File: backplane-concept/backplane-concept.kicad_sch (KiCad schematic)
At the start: 2 parts

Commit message: Rev
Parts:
- removed J2: ~, !footprints:9-1734774-5, symbol 9-1734774-5:PCIE
- added J2: CONN_MINI, CONN_10018784-10201TLF, symbol 10018784-10201TLF:10018784-10201TLF
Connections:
- net RX3 is gone; now on net GND: J1.B23
- net TX2 is gone; now on net GND: J1.B20
- net TX3 is gone; now on net I2C0_ECVT: J1.B22
- net DIR1: no longer J1.A14
- net DIR2: no longer J1.A13
- net ENGHALL2: no longer J1.A20
- net FRBPRESS: no longer J1.B43
- net GND: now also J1.A16, J1.A18, J1.A32; no longer J1.A17, J1.A21, J1.A38, J1.A45, J1.B28, J1.B42
- net PENC_A: no longer J1.A30
- net PENC_B: no longer J1.A32
- net PLDCLK: no longer J1.A24
- net PLDDAT: no longer J1.A25
- net PLOADC1: no longer J1.A22
- net PLOADC2: no longer J1.A23
- net PWM1: no longer J1.A16
- net PWM2: no longer J1.A15
- net RPOT1: no longer J1.B45
- net RPOT2: no longer J1.B46
- net RRBPRESS: no longer J1.B44
- net RRHALL: now also J1.A13; no longer J1.A19
- net SENC_A: no longer J1.A34
- net SENC_B: no longer J1.A36
- net SLDCLK: no longer J1.A28
- net SLDDAT: no longer J1.A29
- net SLOADC1: no longer J1.A26
- net SLOADC2: no longer J1.A27
- net SPARK: no longer J1.A18
- net TEMP1: no longer J1.A49
- net TEMP2: no longer J1.A48
- net TEMP3: no longer J1.A47
- net TEMP4: no longer J1.A46
- net VOLT1: now also J1.A29; no longer J1.B47
- net VOLT2: now also J1.A30; no longer J1.B48
- net VOLT3: now also J1.A31; no longer J1.B49
- net ~PENC_A: no longer J1.A31
- net ~PENC_B: no longer J1.A33
- net ~SENC_A: no longer J1.A35
- net ~SENC_B: no longer J1.A37
- net 3.3V renamed +3V3
- net 5V renamed +5V
- net 8.4V renamed +8V
- net CIPO: no longer names the net of J1.B29
- net COPI: no longer names the net of J1.B30
- net CS1: no longer names the net of J1.B32
- removed net CS2: J1.B33
- removed net CS3: J1.B34
- removed net CS4: J1.B35
- removed net CS5: J1.B36
- removed net CS6: J1.B37
- removed net DIG_OUT: J1.A39
- net I2C_CLK renamed I2C0_DAQ_SCL
- net I2C_DATA renamed I2C0_DAQ_SDA
- removed net IR_AMP: J1.A42
- removed net IR_TEENSY: J1.A41
- removed net N_A: J1.A40
- net RX1 renamed I2C1_DAQ_SCL
- net RX2 renamed I2C0_ECVT
- net RX4: no longer names the net of J1.B25
- net RX5: no longer names the net of J1.B27
- net SCLK: no longer names the net of J1.B31
- net TX1 renamed I2C1_DAQ_SDA
- net TX4: no longer names the net of J1.B24
- net TX5: no longer names the net of J1.B26
- new net ARGB_DAQ: J1.A20
- new net ARGB_ECVT: J1.A19
- new net ARGB_ESP: J1.A21
- new net DAQ_RX0_ECVT_TX0: J1.A15
- new net DAQ_TX0_ECVT_RX0: J1.A14
- new net DAQ_TX1_DATA: J1.A17

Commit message: Backplane Ideas
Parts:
- removed J1: ~, !footprints:9-1734774-5, symbol 9-1734774-5:PCIE
- removed J2: CONN_MINI, CONN_10018784-10201TLF, symbol 10018784-10201TLF:10018784-10201TLF
- added J1: 6473427-1, 64734271, symbol 6473427-1:6473427-1
- added J2, J3, J4: PCIE_8x_Labeled, !footprints:9-1734774-5, symbol !CUSTOM:PCIE_8x_Labeled
- added J5, J6, J7, J8: CONN_MINI, !footprints:10018784-10200TLF, symbol !CUSTOM:PCIE_2x_Labeled
- added U4: ATA6561-GBQW-N, VDFN8_3X3_MCH, symbol ATA6561:ATA6561-GBQW-N
- added U5: ESP32-PICO-D4, Package_DFN_QFN:QFN-48-1EP_7x7mm_P0.5mm_EP5.3x5.3mm, symbol RF_Module:ESP32-PICO-D4
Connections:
- net +3V3: now also J1.B10, J1.B25, J1.B26, J2.A4 (+3V3), J2.A5 (+3V3), J2.A6 (+3V3), J2.B4 (+3V3), J2.B5 (+3V3), J2.B6 (+3V3), J3.A4 (+3V3), J3.A5 (+3V3), J3.A6 (+3V3), J3.B4 (+3V3), J3.B5 (+3V3), J3.B6 (+3V3), J4.A4 (+3V3), J4.A5 (+3V3), J4.A6 (+3V3), J4.B4 (+3V3), J4.B5 (+3V3), J4.B6 (+3V3), J5.A4 (+3V3), J5.A5 (+3V3), J5.A6 (+3V3), J5.B4 (+3V3), J5.B5 (+3V3), J5.B6 (+3V3), J6.A4 (+3V3), J6.A5 (+3V3), J6.A6 (+3V3), J6.B4 (+3V3), J6.B5 (+3V3), J6.B6 (+3V3), J7.A4 (+3V3), J7.A5 (+3V3), J7.A6 (+3V3), J7.B4 (+3V3), J7.B5 (+3V3), J7.B6 (+3V3), J8.A4 (+3V3), J8.A5 (+3V3), J8.A6 (+3V3), J8.B4 (+3V3), J8.B5 (+3V3), J8.B6 (+3V3)
- net +5V: now also J1.A1, J1.A10, J1.A18, J1.A26, J2.A1 (+5V), J2.A2 (+5V), J2.A3 (+5V), J2.B1 (+5V), J2.B2 (+5V), J2.B3 (+5V), J3.A1 (+5V), J3.A2 (+5V), J3.A3 (+5V), J3.B1 (+5V), J3.B2 (+5V), J3.B3 (+5V), J4.A1 (+5V), J4.A2 (+5V), J4.A3 (+5V), J4.B1 (+5V), J4.B2 (+5V), J4.B3 (+5V), J5.A1 (+5V), J5.A2 (+5V), J5.A3 (+5V), J5.B1 (+5V), J5.B2 (+5V), J5.B3 (+5V), J6.A1 (+5V), J6.A2 (+5V), J6.A3 (+5V), J6.B1 (+5V), J6.B2 (+5V), J6.B3 (+5V), J7.A1 (+5V), J7.A2 (+5V), J7.A3 (+5V), J7.B1 (+5V), J7.B2 (+5V), J7.B3 (+5V), J8.A1 (+5V), J8.A2 (+5V), J8.A3 (+5V), J8.B1 (+5V), J8.B2 (+5V), J8.B3 (+5V)
- net +8V: now also J1.B5, J1.B6, J2.A7 (VBATT), J2.A8 (VBATT), J2.B7 (VBATT), J2.B8 (VBATT), J3.A7 (VBATT), J3.A8 (VBATT), J3.B7 (VBATT), J3.B8 (VBATT), J4.A7 (VBATT), J4.A8 (VBATT), J4.B7 (VBATT), J4.B8 (VBATT), J5.A7 (VBATT), J5.A8 (VBATT), J5.B7 (VBATT), J5.B8 (VBATT), J6.A7 (VBATT), J6.A8 (VBATT), J6.B7 (VBATT), J6.B8 (VBATT), J7.A7 (VBATT), J7.A8 (VBATT), J7.B7 (VBATT), J7.B8 (VBATT), J8.A7 (VBATT), J8.A8 (VBATT), J8.B7 (VBATT), J8.B8 (VBATT)
- net CAN_H: now also J2.B12 (CAN_H), J3.B12 (CAN_H), J4.B12 (CAN_H), J5.B12 (CAN_H), J6.B12 (CAN_H), J7.B12 (CAN_H), J8.B12 (CAN_H)
- net CAN_L: now also J2.B13 (CAN_L), J3.B13 (CAN_L), J4.B13 (CAN_L), J5.B13 (CAN_L), J6.B13 (CAN_L), J7.B13 (CAN_L), J8.B13 (CAN_L)
- net DAQ_RX0_ECVT_TX0: now also J2.A13 (DAQ_RX0_ECVT_TX0), J3.A13 (DAQ_RX0_ECVT_TX0), J4.A13 (DAQ_RX0_ECVT_TX0), J5.A13 (DAQ_RX0_ECVT_TX0), J6.A13 (DAQ_RX0_ECVT_TX0), J7.A13 (DAQ_RX0_ECVT_TX0), J8.A13 (DAQ_RX0_ECVT_TX0)
- net DAQ_TX0_ECVT_RX0: now also J2.A12 (DAQ_TX0_ECVT_RX0), J3.A12 (DAQ_TX0_ECVT_RX0), J4.A12 (DAQ_TX0_ECVT_RX0), J5.A12 (DAQ_TX0_ECVT_RX0), J6.A12 (DAQ_TX0_ECVT_RX0), J7.A12 (DAQ_TX0_ECVT_RX0), J8.A12 (DAQ_TX0_ECVT_RX0)
- net DAQ_TX1_DATA: now also J2.A14 (DAQ_TX1_DATA), J3.A14 (DAQ_TX1_DATA), J4.A14 (DAQ_TX1_DATA), J5.A14 (DAQ_TX1_DATA), J6.A14 (DAQ_TX1_DATA), J7.A14 (DAQ_TX1_DATA), J8.A14 (DAQ_TX1_DATA)
- net GND: now also J1.A17, J1.A25, J1.A30, J1.A5, J1.B1, J1.B11, J1.B12, J1.B15, J1.B19, J1.B2, J1.B23, J1.B24, J1.B7, J2.A10 (GND), J2.A11 (GND), J2.A15 (GND), J2.A18 (GND), J2.A28 (GND), J2.A35 (GND), J2.A43 (GND), J2.A9 (GND), J2.B10 (GND), J2.B11 (GND), J2.B18 (GND), J2.B32 (GND), J2.B42 (GND), J2.B43 (GND), J2.B9 (GND), J3.A10 (GND), J3.A11 (GND), J3.A15 (GND), J3.A18 (GND), J3.A28 (GND), J3.A35 (GND), J3.A43 (GND), J3.A9 (GND), J3.B10 (GND), J3.B11 (GND), J3.B18 (GND), J3.B32 (GND), J3.B42 (GND), J3.B43 (GND), J3.B9 (GND), J4.A10 (GND), J4.A11 (GND), J4.A15 (GND), J4.A18 (GND), J4.A28 (GND), J4.A35 (GND), J4.A43 (GND), J4.A9 (GND), J4.B10 (GND), J4.B11 (GND), J4.B18 (GND), J4.B32 (GND), J4.B42 (GND), J4.B43 (GND), J4.B9 (GND), J5.A10 (GND), J5.A11 (GND), J5.A15 (GND), J5.A18 (GND), J5.A9 (GND), J5.B10 (GND), J5.B11 (GND), J5.B18 (GND), J5.B9 (GND), J6.A10 (GND), J6.A11 (GND), J6.A15 (GND), J6.A18 (GND), J6.A9 (GND), J6.B10 (GND), J6.B11 (GND), J6.B18 (GND), J6.B9 (GND), J7.A10 (GND), J7.A11 (GND), J7.A15 (GND), J7.A18 (GND), J7.A9 (GND), J7.B10 (GND), J7.B11 (GND), J7.B18 (GND), J7.B9 (GND), J8.A10 (GND), J8.A11 (GND), J8.A15 (GND), J8.A18 (GND), J8.A9 (GND), J8.B10 (GND), J8.B11 (GND), J8.B18 (GND), J8.B9 (GND)
- net I2C0_DAQ_SCL: now also J2.B15 (I2C0_DAQ_SCL), J3.B15 (I2C0_DAQ_SCL), J4.B15 (I2C0_DAQ_SCL), J5.B15 (I2C0_DAQ_SCL), J6.B15 (I2C0_DAQ_SCL), J7.B15 (I2C0_DAQ_SCL), J8.B15 (I2C0_DAQ_SCL)
- net I2C0_DAQ_SDA: now also J2.B14 (I2C0_DAQ_SDA), J3.B14 (I2C0_DAQ_SDA), J4.B14 (I2C0_DAQ_SDA), J5.B14 (I2C0_DAQ_SDA), J6.B14 (I2C0_DAQ_SDA), J7.B14 (I2C0_DAQ_SDA), J8.B14 (I2C0_DAQ_SDA)
- net I2C1_DAQ_SCL: now also J2.A17 (I2C1_DAQ_SCL), J3.A17 (I2C1_DAQ_SCL), J4.A17 (I2C1_DAQ_SCL), J5.A17 (I2C1_DAQ_SCL), J6.A17 (I2C1_DAQ_SCL), J7.A17 (I2C1_DAQ_SCL), J8.A17 (I2C1_DAQ_SCL)
- net I2C1_DAQ_SDA: now also J2.A16 (I2C1_DAQ_SDA), J3.A16 (I2C1_DAQ_SDA), J4.A16 (I2C1_DAQ_SDA), J5.A16 (I2C1_DAQ_SDA), J6.A16 (I2C1_DAQ_SDA), J7.A16 (I2C1_DAQ_SDA), J8.A16 (I2C1_DAQ_SDA)
- net RPOT1: now also J2.B46 (RPOT1), J3.B46 (RPOT1), J4.B46 (RPOT1)
- net RPOT2: now also J2.B47 (RPOT2), J3.B47 (RPOT2), J4.B47 (RPOT2)
- net SPARK: now also J2.A42 (SPARK), J3.A42 (SPARK), J4.A42 (SPARK)
- new net: U5.1 (VDDA), U5.43 (VDDA), U5.46 (VDDA)
- new net: U5.3 (VDDA3P3), U5.4 (VDDA3P3)
- new net: J2.A19, J3.A19, J4.A19
- new net: J2.A20, J3.A20, J4.A20
- new net: J2.A21, J3.A21, J4.A21
- new net: J2.A22, J3.A22, J4.A22
- new net: J2.A23, J3.A23, J4.A23
- new net: J2.A24, J3.A24, J4.A24
- new net: J2.A25, J3.A25, J4.A25
- new net: J2.A26, J3.A26, J4.A26
- new net: J2.A27, J3.A27, J4.A27
- new net: J2.B19, J3.B19, J4.B19
- new net: J2.B20, J3.B20, J4.B20
- new net: J2.B21, J3.B21, J4.B21
- new net: J2.B22, J3.B22, J4.B22
- new net: J2.B23, J3.B23, J4.B23
- new net: J2.B24, J3.B24, J4.B24
- new net: J2.B25, J3.B25, J4.B25
- new net: J2.B26, J3.B26, J4.B26
- new net: J2.B27, J3.B27, J4.B27
- new net: J2.B48, J3.B48, J4.B48
- new net: J2.B49, J3.B49, J4.B49
- new net AVDD_P: J1.B18
- new net AVDD_S: J1.B22
- new net BP_FRONT: J2.B44 (BP_FRONT), J3.B44 (BP_FRONT), J4.B44 (BP_FRONT)
- new net BP_REAR: J2.B45 (BP_REAR), J3.B45 (BP_REAR), J4.B45 (BP_REAR)
- new net DIR_P: J2.B36 (DIR_P), J3.B36 (DIR_P), J4.B36 (DIR_P)
- new net DIR_S: J2.B38 (DIR_S), J3.B38 (DIR_S), J4.B38 (DIR_S)
- new net ENCA_P: J1.A11, J2.A29 (ENCA_P), J3.A29 (ENCA_P), J4.A29 (ENCA_P)
- new net ENCA_S: J1.A19, J2.A36 (ENCA_S), J3.A36 (ENCA_S), J4.A36 (ENCA_S)
- new net ENCB_P: J1.A13, J2.A31 (ENCB_P), J3.A31 (ENCB_P), J4.A31 (ENCB_P)
- new net ENCB_S: J1.A21, J2.A38 (ENCB_S), J3.A38 (ENCB_S), J4.A38 (ENCB_S)
- new net ENCI_P: J1.A15, J2.A33 (ENCI_P), J3.A33 (ENCI_P), J4.A33 (ENCI_P)
- new net ENCI_S: J1.A23, J2.A40 (ENCI_S), J3.A40 (ENCI_S), J4.A40 (ENCI_S)
- new net HALL1_P: J1.A2
- new net HALL1_S: J1.A27
- new net HALL2_P: J1.A3
- new net HALL2_S: J1.A28
- new net HALL3_P: J1.A4
- new net HALL3_S: J1.A29
- new net HALL_ENG1: J1.B3, J2.B33 (HALL_ENG1), J3.B33 (HALL_ENG1), J4.B33 (HALL_ENG1)
- new net HALL_ENG2: J1.B4, J2.B41 (HALL_ENG2), J3.B41 (HALL_ENG2), J4.B41 (HALL_ENG2)
- new net HALL_RW: J2.B34 (HALL_RW), J3.B34 (HALL_RW), J4.B34 (HALL_RW)
- new net I2C0_ECVT_SCL: J2.B17 (I2C0_ECVT_SCL), J3.B17 (I2C0_ECVT_SCL), J4.B17 (I2C0_ECVT_SCL), J5.B17 (I2C0_ECVT_SCL), J6.B17 (I2C0_ECVT_SCL), J7.B17 (I2C0_ECVT_SCL), J8.B17 (I2C0_ECVT_SCL)
- new net I2C0_ECVT_SDA: J2.B16 (I2C0_ECVT_SDA), J3.B16 (I2C0_ECVT_SDA), J4.B16 (I2C0_ECVT_SDA), J5.B16 (I2C0_ECVT_SDA), J6.B16 (I2C0_ECVT_SDA), J7.B16 (I2C0_ECVT_SDA), J8.B16 (I2C0_ECVT_SDA)
- new net I2C1_ECVT_EXT_SCL: J1.B9, J2.B40 (I2C1_ECVT_EXT_SCL), J3.B40 (I2C1_ECVT_EXT_SCL), J4.B40 (I2C1_ECVT_EXT_SCL)
- new net I2C1_ECVT_EXT_SDA: J1.B8, J2.B39 (I2C1_ECVT_EXT_SDA), J3.B39 (I2C1_ECVT_EXT_SDA), J4.B39 (I2C1_ECVT_EXT_SDA)
- new net IN+_P: J1.B16
- new net IN+_S: J1.B20
- new net IN-_P: J1.B17
- new net IN-_S: J1.B21
- new net LOADC_CLK_P: J2.B28 (LOADC_CLK_P), J2.B30 (LOADC_CLK_S), J3.B28 (LOADC_CLK_P), J3.B30 (LOADC_CLK_S), J4.B28 (LOADC_CLK_P), J4.B30 (LOADC_CLK_S)
- new net LOADC_DAT_P: J2.B29 (LOADC_DAT_P), J3.B29 (LOADC_DAT_P), J4.B29 (LOADC_DAT_P)
- new net LOADC_DAT_S: J2.B31 (LOADC_DAT_S), J3.B31 (LOADC_DAT_S), J4.B31 (LOADC_DAT_S)
- new net MOT1_P: J1.A7
- new net MOT1_S: J1.A32
- new net MOT2_P: J1.A8
- new net MOT2_S: J1.A33
- new net MOT3_P: J1.A9
- new net MOT3_S: J1.A34
- new net PWM_P: J2.B35 (PWM_P), J3.B35 (PWM_P), J4.B35 (PWM_P)
- new net PWM_S: J2.B37 (PWM_S), J3.B37 (PWM_S), J4.B37 (PWM_S)
- new net THERM_A1_CASE: J1.B13, J2.A46 (THERM_A1_CASE), J3.A46 (THERM_A1_CASE), J4.A46 (THERM_A1_CASE)
- new net THERM_A2_CASE: J1.B14, J2.A47 (THERM_A2_CASE), J3.A47 (THERM_A2_CASE), J4.A47 (THERM_A2_CASE)
- new net THERM_A3: J2.A48 (THERM_A3), J3.A48 (THERM_A3), J4.A48 (THERM_A3)
- new net THERM_A4: J2.A49 (THERM_A4), J3.A49 (THERM_A4), J4.A49 (THERM_A4)
- new net THERM_P: J1.A6, J2.A44 (THERM_P), J3.A44 (THERM_P), J4.A44 (THERM_P)
- new net THERM_S: J1.A31, J2.A45 (THERM_S), J3.A45 (THERM_S), J4.A45 (THERM_S)
- new net ~ENCA_P: J1.A12, J2.A30 (~ENCA_P), J3.A30 (~ENCA_P), J4.A30 (~ENCA_P)
- new net ~ENCA_S: J1.A20, J2.A37 (~ENCA_S), J3.A37 (~ENCA_S), J4.A37 (~ENCA_S)
- new net ~ENCB_P: J1.A14, J2.A32 (~ENCB_P), J3.A32 (~ENCB_P), J4.A32 (~ENCB_P)
- new net ~ENCB_S: J1.A22, J2.A39 (~ENCB_S), J3.A39 (~ENCB_S), J4.A39 (~ENCB_S)
- new net ~ENCI_P: J1.A16, J2.A34 (~ENCI_P), J3.A34 (~ENCI_P), J4.A34 (~ENCI_P)
- new net ~ENCI_S: J1.A24, J2.A41 (~ENCI_S), J3.A41 (~ENCI_S), J4.A41 (~ENCI_S)
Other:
- added sheet Analog Frontend (analog_frontend.kicad_sch)

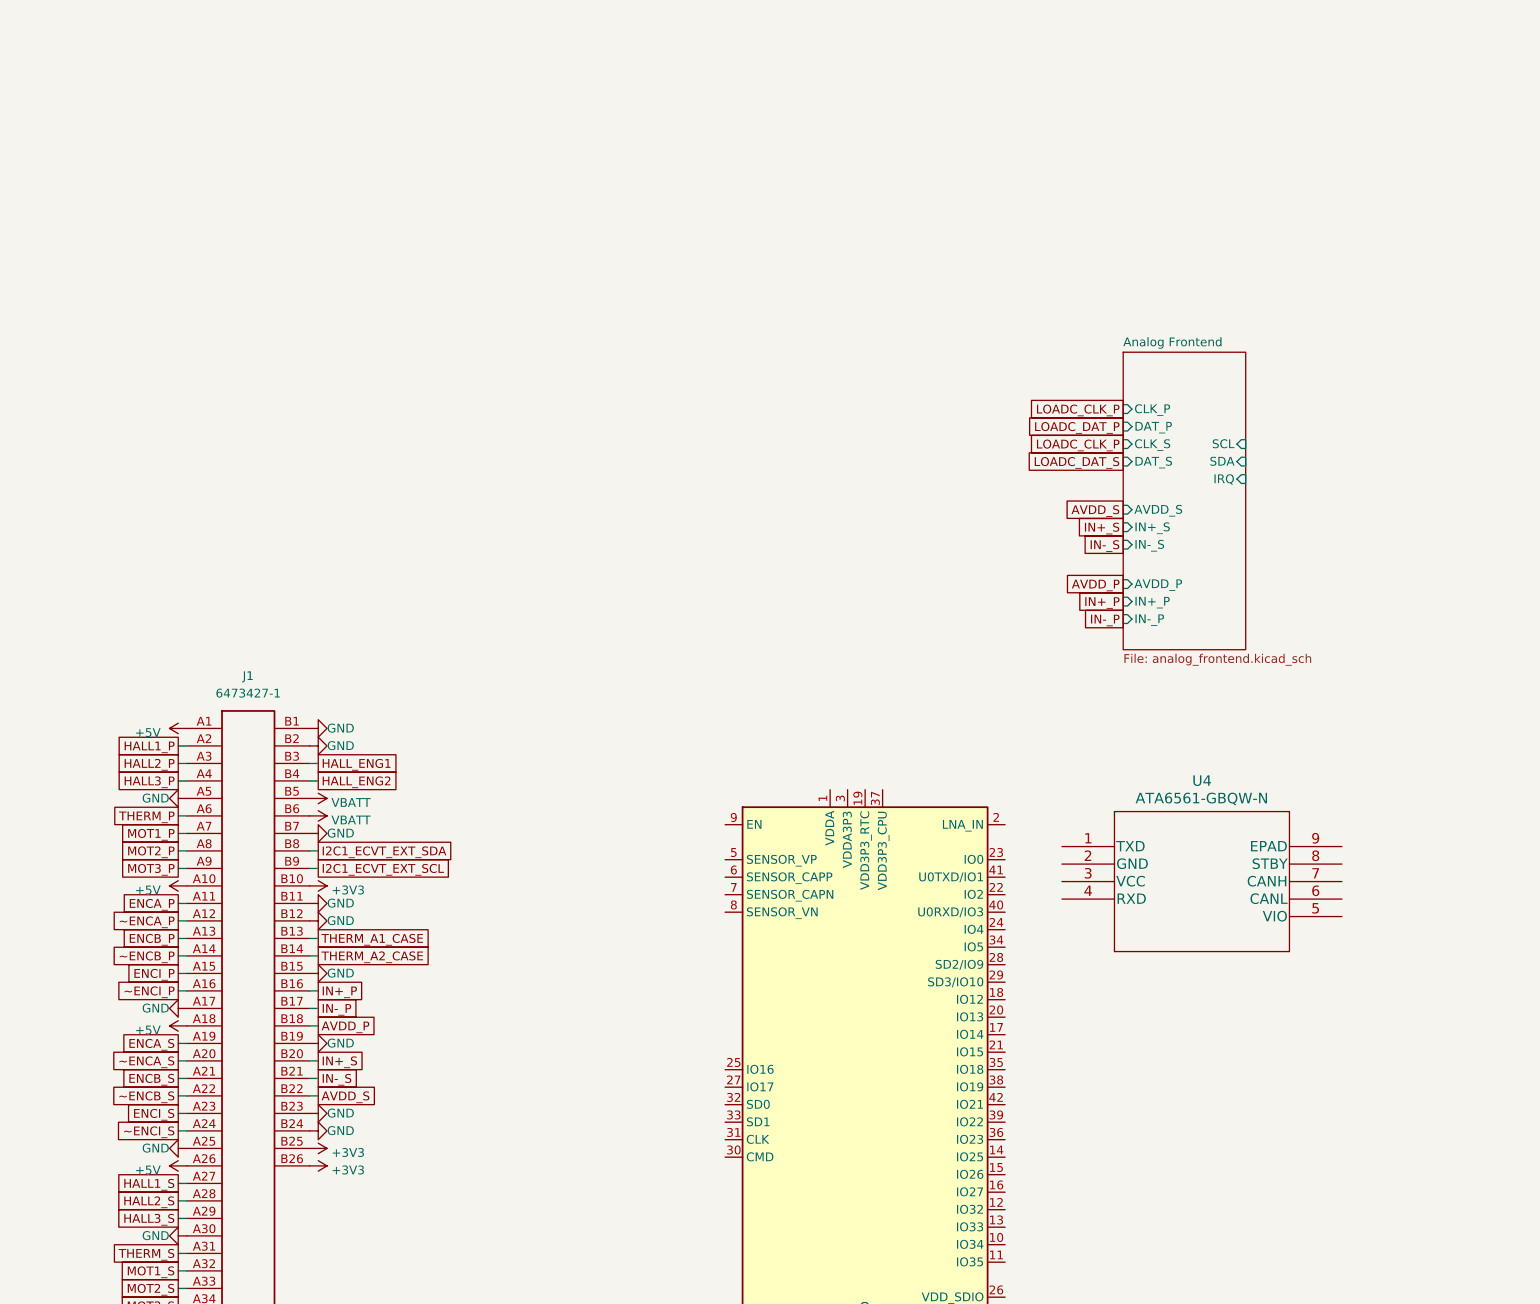
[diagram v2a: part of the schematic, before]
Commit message: Design PSUs, route bucks
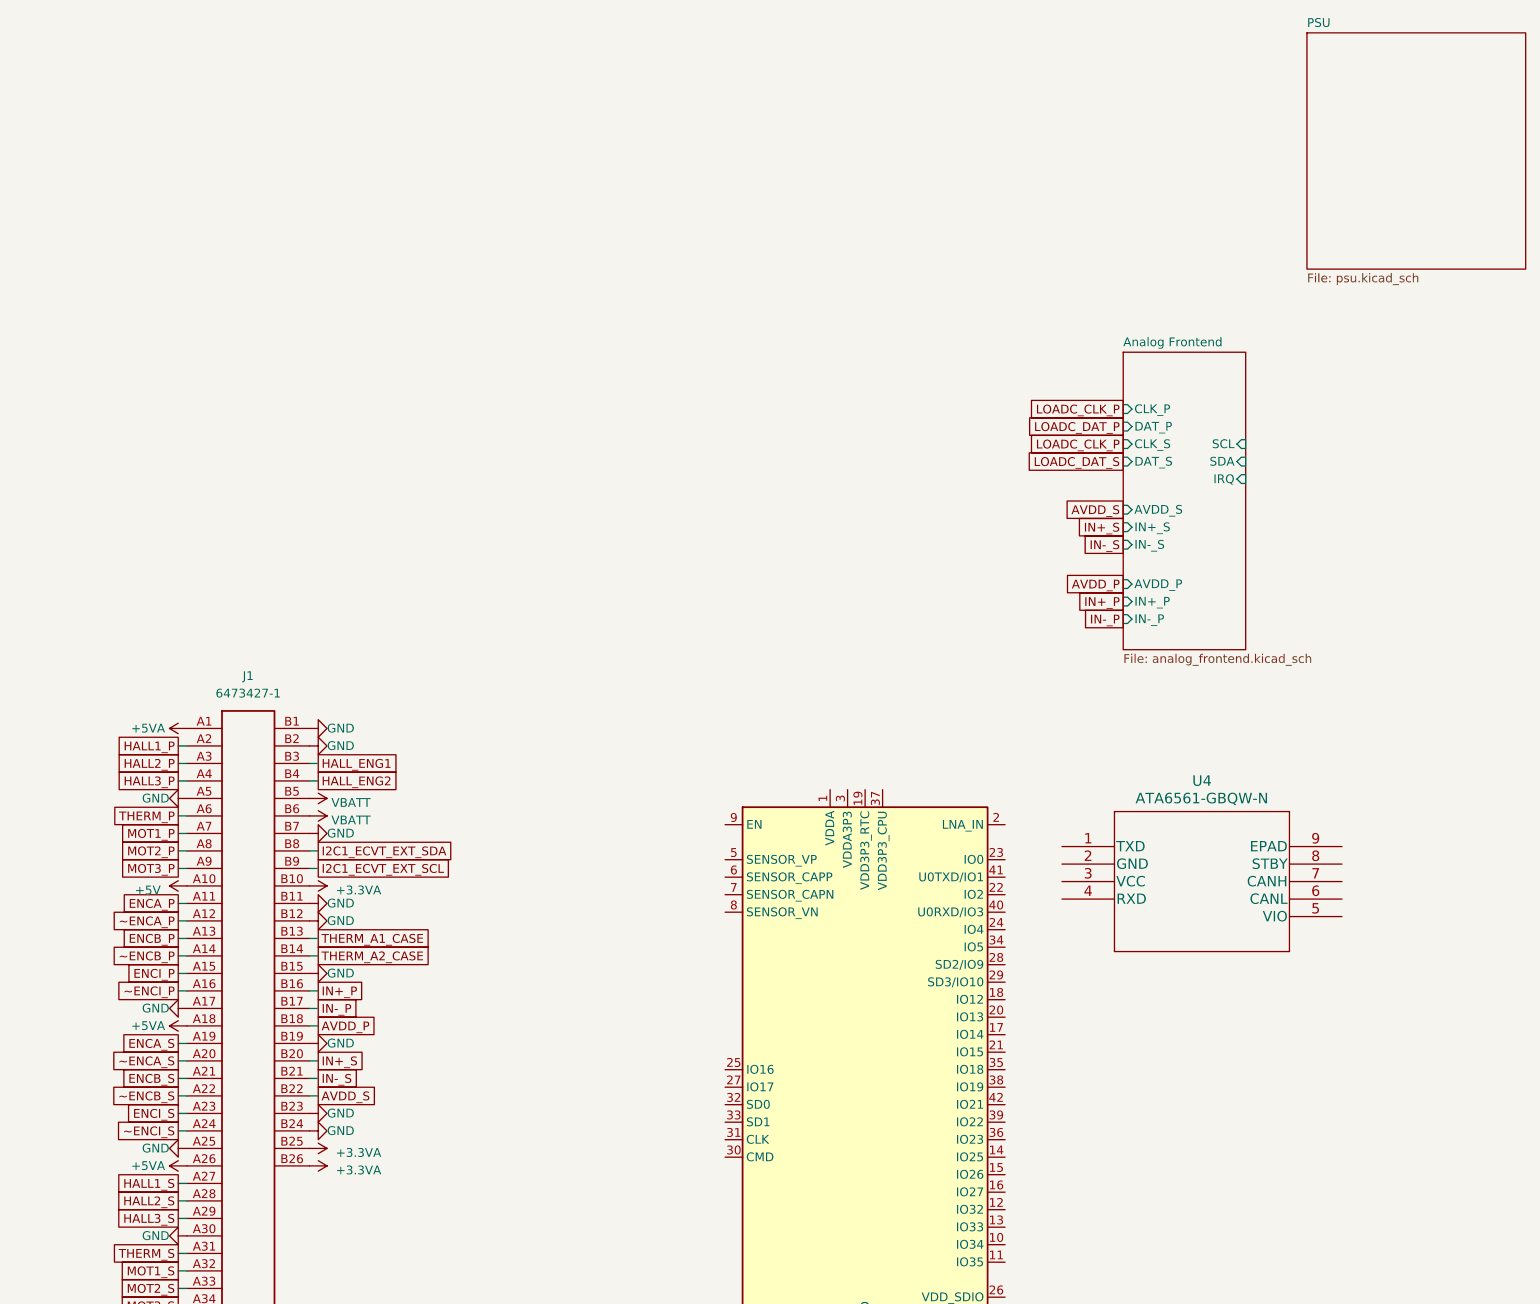
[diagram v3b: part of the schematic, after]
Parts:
- J1: footprint 64734271 -> !footprints:64734271
- U4: footprint VDFN8_3X3_MCH -> !footprints:ATA6561-GBQW-N
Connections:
- net +3V3: no longer J1.B10, J1.B25, J1.B26
- net +5V: no longer J1.A1, J1.A18, J1.A26
- new net +3.3VA: J1.B10, J1.B25, J1.B26
- new net +5VA: J1.A1, J1.A18, J1.A26
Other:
- added sheet PSU (psu.kicad_sch)

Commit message: Add testpoints
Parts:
- added TP1: PCLK, !footprints:TestPoint_Pad_D1.0mm, symbol Connector:TestPoint_Small
- added TP12: HENG1, !footprints:TestPoint_Pad_D1.0mm, symbol Connector:TestPoint_Small
- added TP13: HENG2, !footprints:TestPoint_Pad_D1.0mm, symbol Connector:TestPoint_Small
- added TP14: BPF, !footprints:TestPoint_Pad_D1.0mm, symbol Connector:TestPoint_Small
- added TP15: BPR, !footprints:TestPoint_Pad_D1.0mm, symbol Connector:TestPoint_Small
- added TP16: RP1, !footprints:TestPoint_Pad_D1.0mm, symbol Connector:TestPoint_Small
- added TP17: RP2, !footprints:TestPoint_Pad_D1.0mm, symbol Connector:TestPoint_Small
- added TP18: HRW, !footprints:TestPoint_Pad_D1.0mm, symbol Connector:TestPoint_Small
- added TP19: PP, !footprints:TestPoint_Pad_D1.0mm, symbol Connector:TestPoint_Small
- added TP2: PDAT, !footprints:TestPoint_Pad_D1.0mm, symbol Connector:TestPoint_Small
- added TP20: DP, !footprints:TestPoint_Pad_D1.0mm, symbol Connector:TestPoint_Small
- added TP21: PS, !footprints:TestPoint_Pad_D1.0mm, symbol Connector:TestPoint_Small
- added TP22: DS, !footprints:TestPoint_Pad_D1.0mm, symbol Connector:TestPoint_Small
- added TP23: TP, !footprints:TestPoint_Pad_D1.0mm, symbol Connector:TestPoint_Small
- added TP24: TS, !footprints:TestPoint_Pad_D1.0mm, symbol Connector:TestPoint_Small
- added TP25: TA1, !footprints:TestPoint_Pad_D1.0mm, symbol Connector:TestPoint_Small
- added TP26: TA2, !footprints:TestPoint_Pad_D1.0mm, symbol Connector:TestPoint_Small
- added TP27: TA3, !footprints:TestPoint_Pad_D1.0mm, symbol Connector:TestPoint_Small
- added TP28: TA4, !footprints:TestPoint_Pad_D1.0mm, symbol Connector:TestPoint_Small
- added TP29: SPK, !footprints:TestPoint_Pad_D1.0mm, symbol Connector:TestPoint_Small
- added TP3: SCLK, !footprints:TestPoint_Pad_D1.0mm, symbol Connector:TestPoint_Small
- added TP30: EAS, !footprints:TestPoint_Pad_D1.0mm, symbol Connector:TestPoint_Small
- added TP31: EBS, !footprints:TestPoint_Pad_D1.0mm, symbol Connector:TestPoint_Small
- added TP32: EIS, !footprints:TestPoint_Pad_D1.0mm, symbol Connector:TestPoint_Small
- added TP33: EAP, !footprints:TestPoint_Pad_D1.0mm, symbol Connector:TestPoint_Small
- added TP34: EBP, !footprints:TestPoint_Pad_D1.0mm, symbol Connector:TestPoint_Small
- added TP35: EIP, !footprints:TestPoint_Pad_D1.0mm, symbol Connector:TestPoint_Small
- added TP36: DI1C, !footprints:TestPoint_Pad_D1.0mm, symbol Connector:TestPoint_Small
- added TP37: DI1D, !footprints:TestPoint_Pad_D1.0mm, symbol Connector:TestPoint_Small
- added TP38: DI0D, !footprints:TestPoint_Pad_D1.0mm, symbol Connector:TestPoint_Small
- added TP39: DI0C, !footprints:TestPoint_Pad_D1.0mm, symbol Connector:TestPoint_Small
- added TP4: SDAT, !footprints:TestPoint_Pad_D1.0mm, symbol Connector:TestPoint_Small
- added TP40: CANH, !footprints:TestPoint_Pad_D1.0mm, symbol Connector:TestPoint_Small
- added TP41: CANL, !footprints:TestPoint_Pad_D1.0mm, symbol Connector:TestPoint_Small
- added TP42: EI0D, !footprints:TestPoint_Pad_D1.0mm, symbol Connector:TestPoint_Small
- added TP43: EI0C, !footprints:TestPoint_Pad_D1.0mm, symbol Connector:TestPoint_Small
- added TP44: DRET, !footprints:TestPoint_Pad_D1.0mm, symbol Connector:TestPoint_Small
- added TP45: DTD, !footprints:TestPoint_Pad_D1.0mm, symbol Connector:TestPoint_Small
- added TP46: DTER, !footprints:TestPoint_Pad_D1.0mm, symbol Connector:TestPoint_Small
- added TP5: SAVDD, !footprints:TestPoint_Pad_D1.0mm, symbol Connector:TestPoint_Small
- added TP6: PAVDD, !footprints:TestPoint_Pad_D1.0mm, symbol Connector:TestPoint_Small
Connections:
- net AVDD_P: now also TP6.1
- net AVDD_S: now also TP5.1
- net BP_FRONT: now also TP14.1
- net BP_REAR: now also TP15.1
- net CAN_H: now also TP40.1
- net CAN_L: now also TP41.1
- net DAQ_RX0_ECVT_TX0: now also TP44.1
- net DAQ_TX0_ECVT_RX0: now also TP46.1
- net DAQ_TX1_DATA: now also TP45.1
- net DIR_P: now also TP20.1
- net DIR_S: now also TP22.1
- net ENCA_P: now also TP33.1
- net ENCA_S: now also TP30.1
- net ENCB_P: now also TP34.1
- net ENCB_S: now also TP31.1
- net ENCI_P: now also TP35.1
- net ENCI_S: now also TP32.1
- net HALL_ENG1: now also TP12.1
- net HALL_ENG2: now also TP13.1
- net HALL_RW: now also TP18.1
- net I2C0_DAQ_SCL: now also TP39.1
- net I2C0_DAQ_SDA: now also TP38.1
- net I2C0_ECVT_SCL: now also TP43.1
- net I2C0_ECVT_SDA: now also TP42.1
- net I2C1_DAQ_SCL: now also TP36.1
- net I2C1_DAQ_SDA: now also TP37.1
- net LOADC_CLK_P: now also TP1.1
- net LOADC_DAT_P: now also TP2.1
- net LOADC_DAT_S: now also TP4.1
- net PWM_P: now also TP19.1
- net PWM_S: now also TP21.1
- net RPOT1: now also TP16.1
- net RPOT2: now also TP17.1
- net SPARK: now also TP29.1
- net THERM_A1_CASE: now also TP25.1
- net THERM_A2_CASE: now also TP26.1
- net THERM_A3: now also TP27.1
- net THERM_A4: now also TP28.1
- net THERM_P: now also TP23.1
- net THERM_S: now also TP24.1
- new net LOADC_CLK_S: TP3.1
